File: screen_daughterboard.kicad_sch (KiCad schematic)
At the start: 18 parts, among them J7 Conn_01x24_Socket, Q4 Si1308EDL

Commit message: fixed page numbers
and adjusted some label types
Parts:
- renumbered C54 to C40, C55 to C41, C56 to C42, C57 to C43, C58 to C44, C59 to C45, C60 to C46, C61 to C47, C62 to C48, C63 to C49, D5 to D1, D6 to D2, D7 to D3, J7 to J6, L2 to L1, Q4 to Q3, R33 to R21, R34 to R23
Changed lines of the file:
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@@
+	(wire
+		(pts
+			(xy 68.58 34.29) (xy 74.93 34.29)
+		)
+		(stroke
+			(width 0)
+			(type default)
+		)
+	)
 	(wire
 		(pts
@@
 	(wire
 		(pts
+			(xy 68.58 31.75) (xy 74.93 31.75)
+		)
+		(stroke
+			(width 0)
+			(type default)
+		)
+	)
+	(wire
+		(pts
 			(xy 115.57 34.29) (xy 118.11 34.29)
 		)
@@
 	(wire
 		(pts
+			(xy 66.04 85.09) (xy 74.93 85.09)
+		)
+		(stroke
+			(width 0)
+			(type default)
+		)
+	)
+	(wire
+		(pts
 			(xy 53.34 39.37) (xy 74.93 39.37)
 		)
@@
 	(wire
 		(pts
-			(xy 132.08 41.91) (xy 130.81 41.91)
+			(xy 132.08 41.91) (xy 125.73 41.91)
 		)
 		(stroke
@@
 	(wire
 		(pts
-			(xy 175.26 81.28) (xy 176.53 81.28)
+			(xy 167.64 81.28) (xy 176.53 81.28)
 		)
 		(stroke
@@
 	(wire
 		(pts
-			(xy 146.05 71.12) (xy 147.32 71.12)
+			(xy 66.04 80.01) (xy 74.93 80.01)
+		)
+		(stroke
+			(width 0)
+			(type default)
+		)
+	)
+	(wire
+		(pts
+			(xy 137.16 71.12) (xy 147.32 71.12)
 		)
 		(stroke
@@
 	(wire
 		(pts
-			(xy 142.24 48.26) (xy 140.97 48.26)
+			(xy 147.32 48.26) (xy 140.97 48.26)
 		)
 		(stroke
@@
 		)
 	)
-	(hierarchical_label "PREVGH"
-		(shape input)
-		(at 74.93 80.01 180)
+	(label "GDR"
+		(at 125.73 41.91 0)
 		(effects
 			(font
 				(size 1.27 1.27)
 			)
-			(justify right)
-		)
-	)
-	(hierarchical_label "PREVGH"
-		(shape input)
-		(at 146.05 71.12 180)
+			(justify left bottom)
+		)
+	)
+	(label "RESE"
+		(at 147.32 48.26 180)
 		(effects
 			(font
 				(size 1.27 1.27)
 			)
-			(justify right)
+			(justify right bottom)
+		)
+	)
+	(label "PREVGH"
+		(at 66.04 80.01 0)
+		(effects
+			(font
+				(size 1.27 1.27)
+			)
+			(justify left bottom)
+		)
+	)
+	(label "PREVGL"
+		(at 167.64 81.28 0)
+		(effects
+			(font
+				(size 1.27 1.27)
+			)
+			(justify left bottom)
+		)
+	)
+	(label "RESE"
+		(at 68.58 34.29 0)
+		(effects
+			(font
+				(size 1.27 1.27)
+			)
+			(justify left bottom)
+		)
+	)
+	(label "PREVGH"
+		(at 137.16 71.12 0)
+		(effects
+			(font
+				(size 1.27 1.27)
+			)
+			(justify left bottom)
+		)
+	)
+	(label "PREVGL"
+		(at 66.04 85.09 0)
+		(effects
+			(font
+				(size 1.27 1.27)
+			)
+			(justify left bottom)
+		)
+	)
+	(label "GDR"
+		(at 68.58 31.75 0)
+		(effects
+			(font
+				(size 1.27 1.27)
+			)
+			(justify left bottom)
 		)
 	)
@@
 		)
 	)
-	(hierarchical_label "RESE"
-		(shape input)
-		(at 74.93 34.29 180)
-		(effects
-			(font
-				(size 1.27 1.27)
-			)
-			(justify right)
-		)
-	)
 	(hierarchical_label "GND"
-		(shape input)
+		(shape bidirectional)
 		(at 114.3 41.91 180)
 		(effects
@@
 		)
 	)
-	(hierarchical_label "RESE"
-		(shape input)
-		(at 142.24 48.26 0)
-		(effects
-			(font
-				(size 1.27 1.27)
-			)
-			(justify left)
-		)
-	)
-	(hierarchical_label "GDR"
-		(shape input)
-		(at 74.93 31.75 180)
-		(effects
-			(font
-				(size 1.27 1.27)
-			)
-			(justify right)
-		)
-	)
 	(hierarchical_label "DISPLAY_BUSY"
-		(shape input)
+		(shape output)
 		(at 74.93 49.53 180)
 		(effects
@@
 		)
 	)
-	(hierarchical_label "PREVGL"
-		(shape input)
-		(at 74.93 85.09 180)
-		(effects
-			(font
-				(size 1.27 1.27)
-			)
-			(justify right)
-		)
-	)
 	(hierarchical_label "DISPLAY_CS"
 		(shape input)
@@
 	)
 	(hierarchical_label "GND"
-		(shape input)
+		(shape bidirectional)
 		(at 38.1 87.63 180)
 		(effects
@@
 		)
 	)
-	(hierarchical_label "PREVGL"
-		(shape input)
-		(at 175.26 81.28 180)
-		(effects
-			(font
-				(size 1.27 1.27)
-			)
-			(justify right)
-		)
-	)
-	(hierarchical_label "GDR"
-		(shape input)
-		(at 130.81 41.91 180)
-		(effects
-			(font
-				(size 1.27 1.27)
-			)
-			(justify right)
-		)
-	)
 	(symbol
 		(lib_id "Diode:MBR0530")
@@
 		(on_board yes)
 		(dnp no)
-		(property "Reference" "D5"
+		(property "Reference" "D1"
 			(at 148.59 69.596 0)
 			(effects
@@
 		(dnp no)
 		(fields_autoplaced yes)
-		(property "Reference" "R33"
+		(property "Reference" "R21"
 			(at 134.62 50.7999 0)
 			(effects
@@
 		(dnp no)
 		(fields_autoplaced yes)
-		(property "Reference" "C60"
+		(property "Reference" "C46"
 			(at 118.11 36.8235 0)
 			(effects
@@
 		(dnp no)
 		(fields_autoplaced yes)
-		(property "Reference" "J7"
+		(property "Reference" "J6"
 			(at 81.28 57.1499 0)
 			(effects
@@
 		(dnp no)
 		(fields_autoplaced yes)
-		(property "Reference" "#PWR099"
+		(property "Reference" "#PWR075"
 			(at 147.32 86.36 0)
 			(effects
@@
 		(dnp no)
 		(fields_autoplaced yes)
-		(property "Reference" "#PWR094"
+		(property "Reference" "#PWR073"
 			(at 115.57 49.53 0)
 			(effects
@@
 		(dnp no)
 		(fields_autoplaced yes)
-		(property "Reference" "#PWR0100"
+		(property "Reference" "#PWR076"
 			(at 157.48 88.9 0)
 			(effects
@@
 		(dnp no)
 		(fields_autoplaced yes)
-		(property "Reference" "C56"
+		(property "Reference" "C42"
 			(at 49.5363 76.2 90)
 			(effects
@@
 		(dnp no)
 		(fields_autoplaced yes)
-		(property "Reference" "C59"
+		(property "Reference" "C45"
 			(at 57.1563 81.28 90)
 			(effects
@@
 		(dnp no)
 		(fields_autoplaced yes)
-		(property "Reference" "L2"
+		(property "Reference" "L1"
 			(at 120.65 29.21 90)
 			(effects
@@
 		(dnp no)
 		(fields_autoplaced yes)
-		(property "Reference" "C58"
+		(property "Reference" "C44"
 			(at 57.1563 71.12 90)
 			(effects
@@
 		(dnp no)
 		(fields_autoplaced yes)
-		(property "Reference" "R34"
+		(property "Reference" "R23"
 			(at 143.51 50.7999 0)
 			(effects
@@
 		(on_board yes)
 		(dnp no)
-		(property "Reference" "D7"
+		(property "Reference" "D3"
 			(at 178.562 79.502 0)
 			(effects
@@
 		(dnp no)
 		(fields_autoplaced yes)
-		(property "Reference" "Q4"
+		(property "Reference" "Q3"
 			(at 144.78 40.6399 0)
 			(effects
@@
 		(dnp no)
 		(fields_autoplaced yes)
-		(property "Reference" "C61"
+		(property "Reference" "C47"
 			(at 149.86 73.6535 0)
 			(effects
@@
 		(dnp no)
 		(fields_autoplaced yes)
-		(property "Reference" "C62"
+		(property "Reference" "C48"
 			(at 160.02 63.4935 0)
 			(effects
@@
 		(dnp no)
 		(fields_autoplaced yes)
-		(property "Reference" "#PWR098"
+		(property "Reference" "#PWR074"
 			(at 140.97 63.5 0)
 			(effects
@@
 		(on_board yes)
 		(dnp no)
-		(property "Reference" "D6"
+		(property "Reference" "D2"
 			(at 158.75 81.026 0)
 			(effects
@@
 		(dnp no)
 		(fields_autoplaced yes)
-		(property "Reference" "C63"
+		(property "Reference" "C49"
 			(at 179.07 83.8135 0)
 			(effects
@@
 		(dnp no)
 		(fields_autoplaced yes)
-		(property "Reference" "#PWR089"
+		(property "Reference" "#PWR065"
 			(at 55.88 63.5 0)
 			(effects
@@
 		(dnp no)
 		(fields_autoplaced yes)
-		(property "Reference" "C55"
+		(property "Reference" "C41"
 			(at 49.5363 66.04 90)
 			(effects
@@
 		(dnp no)
 		(fields_autoplaced yes)
-		(property "Reference" "#PWR091"
+		(property "Reference" "#PWR072"
 			(at 119.38 33.02 0)
 			(effects
@@
 		(dnp no)
 		(fields_autoplaced yes)
-		(property "Reference" "#PWR0101"
+		(property "Reference" "#PWR077"
 			(at 176.53 96.52 0)
 			(effects
@@
 		(dnp no)
 		(fields_autoplaced yes)
-		(property "Reference" "C57"
+		(property "Reference" "C43"
 			(at 50.8063 33.02 90)
 			(effects
@@
 		(dnp no)
 		(fields_autoplaced yes)
-		(property "Reference" "#PWR088"
+		(property "Reference" "#PWR050"
 			(at 39.37 96.52 0)
 			(effects
@@
 		(dnp no)
 		(fields_autoplaced yes)
-		(property "Reference" "C54"
+		(property "Reference" "C40"
 			(at 45.7263 58.42 90)
 			(effects

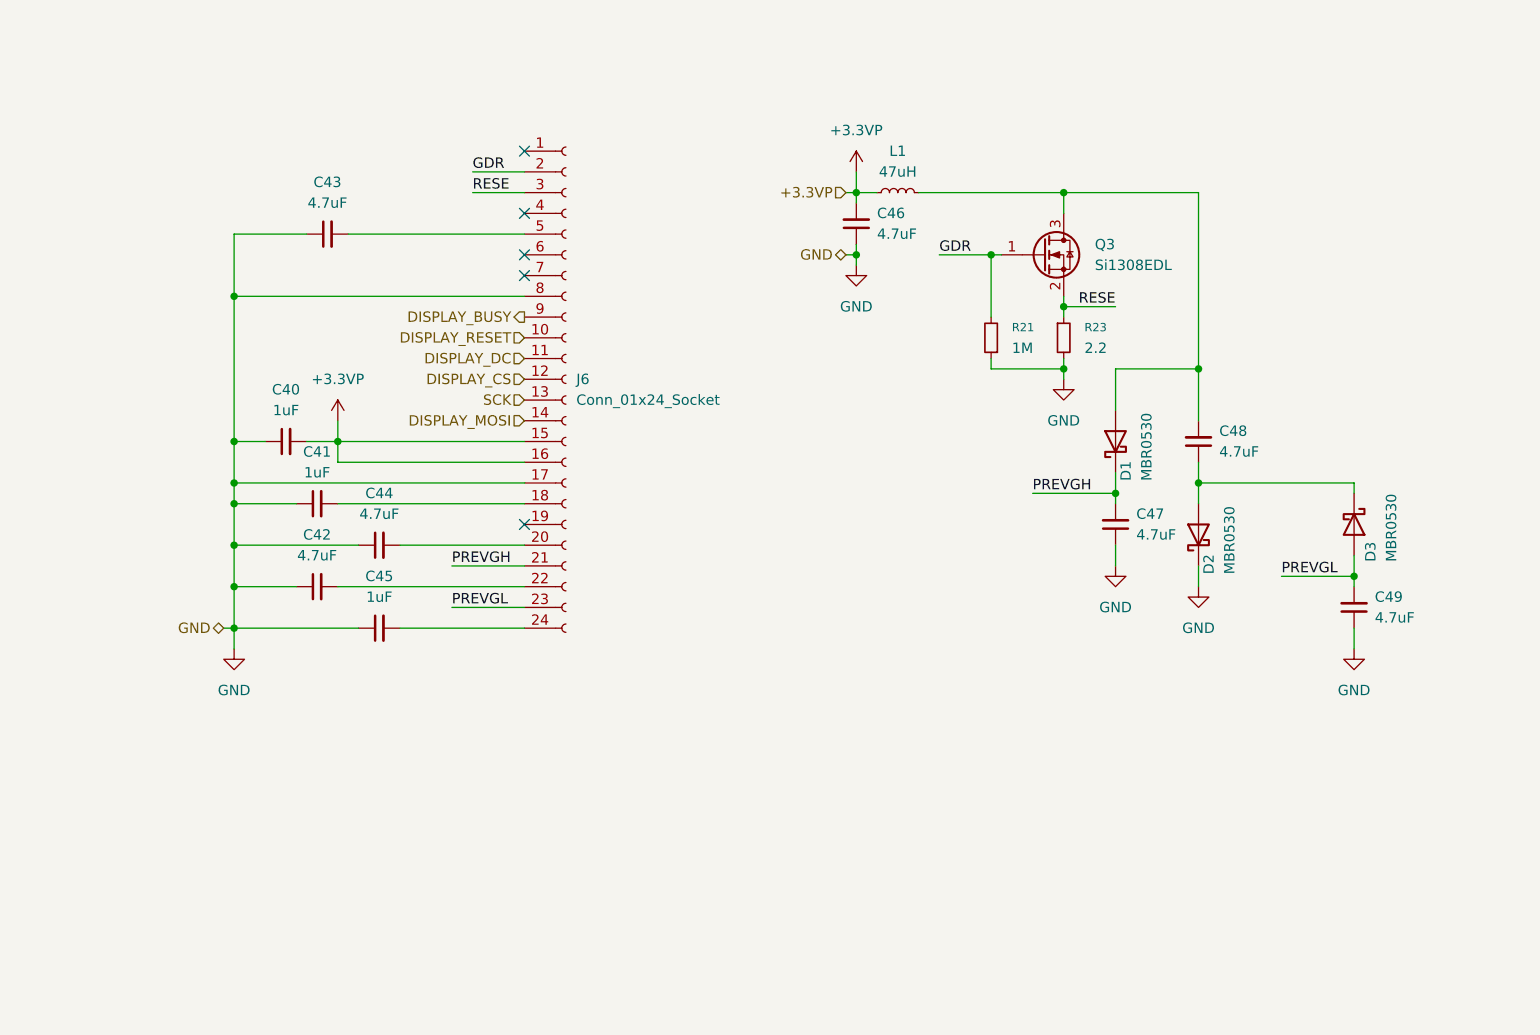
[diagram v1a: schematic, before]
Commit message: separating schematics based on board
finished splitting every component up into separate sheets in the schematic based on what physical board it's going on
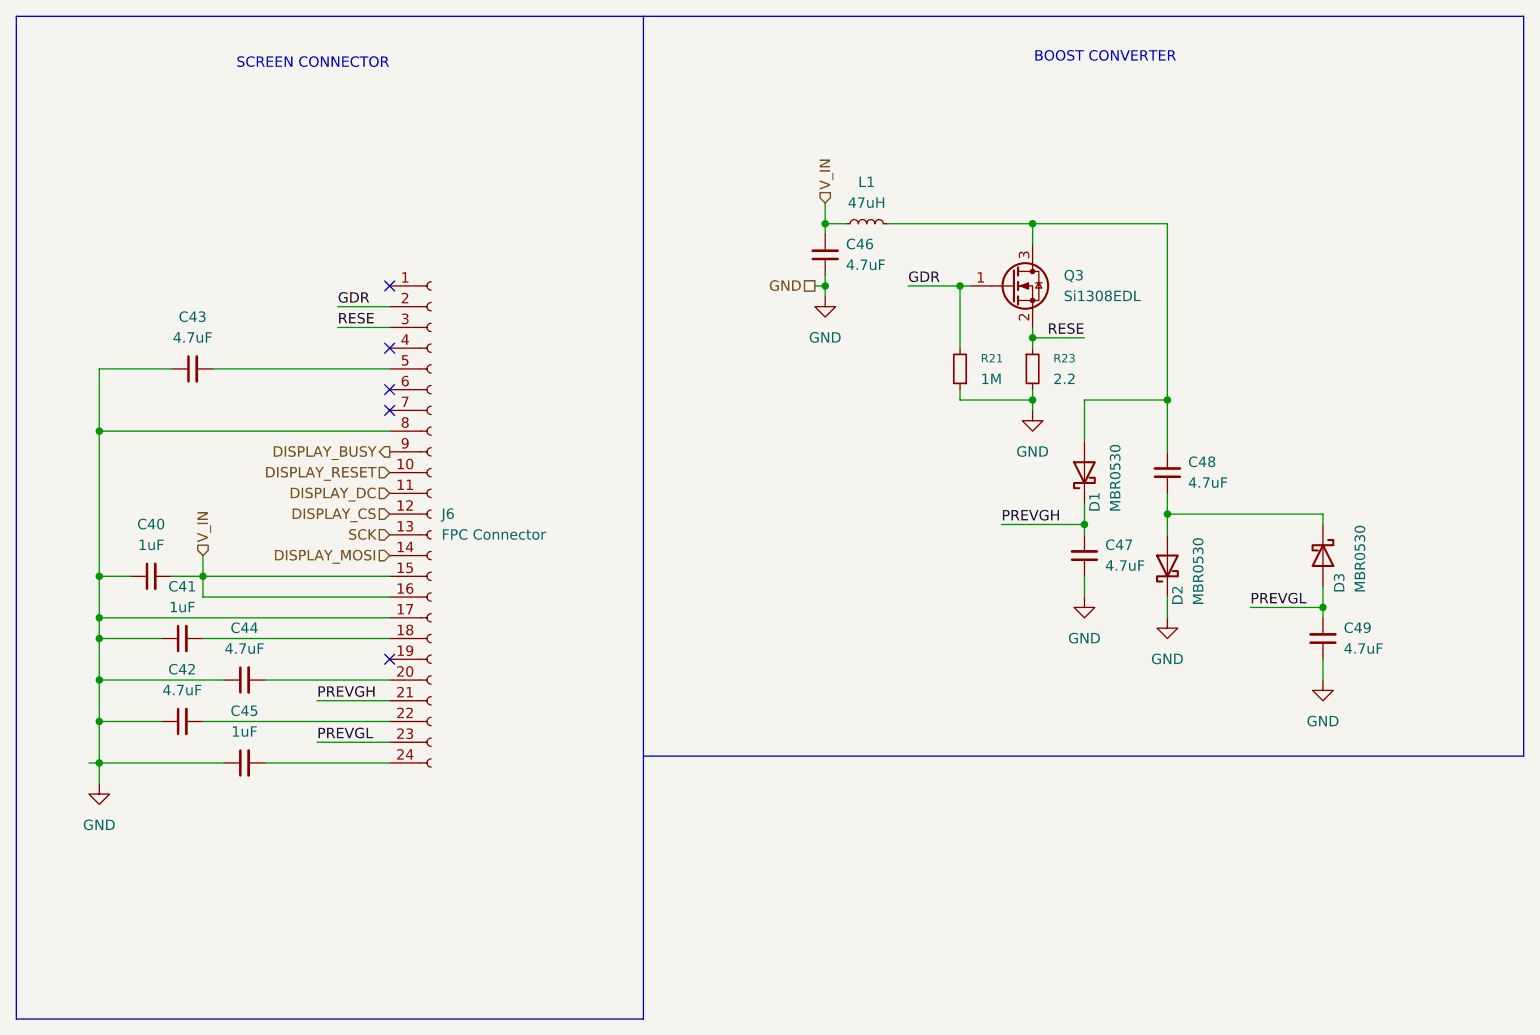
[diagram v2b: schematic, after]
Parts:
- J6: value Conn_01x24_Socket -> FPC Connector
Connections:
- net +3.3VP renamed V_IN
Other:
- note added: "BOOST CONVERTER"
- note added: "SCREEN CONNECTOR"
- moved on the sheet: C40, C41, C42, C43, C44, C45, C46, C47, C48, C49, D1, D2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

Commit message: assigning pcb footprints
assigned pcb footprints to most components:

- rotary encoder footprint will need slight modification to fit bourns PEC11L

- need to finalize components for reset button and the four switches before assigning those footprints
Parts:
- C40, C41, C42, C43, C44, C45, C46, C47, C48, C49: footprint (none) -> Capacitor_SMD:C_0805_2012Metric
- J6: footprint (none) -> Connector_FFC-FPC:Hirose_FH12-24S-0.5SH_1x24-1MP_P0.50mm_Horizontal
- L1: footprint (none) -> Inductor_SMD:L_APV_ANR3015
- R21: footprint (none) -> Resistor_SMD:R_0805_2012Metric
- R23: footprint (none) -> Resistor_SMD:R_0603_1608Metric
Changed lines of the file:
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@@
 			)
 		)
-		(property "Footprint" ""
+		(property "Footprint" "Resistor_SMD:R_0805_2012Metric"
 			(at 128.27 55.88 0)
 			(effects
@@
 			)
 		)
-		(property "Footprint" ""
+		(property "Footprint" "Capacitor_SMD:C_0805_2012Metric"
 			(at 111.76 41.91 0)
 			(effects
@@
 			)
 		)
-		(property "Footprint" ""
+		(property "Footprint" "Connector_FFC-FPC:Hirose_FH12-24S-0.5SH_1x24-1MP_P0.50mm_Horizontal"
 			(at 63.5 73.66 0)
 			(effects
@@
 			)
 		)
-		(property "Footprint" ""
+		(property "Footprint" "Capacitor_SMD:C_0805_2012Metric"
 			(at 33.02 99.06 0)
 			(effects
@@
 			)
 		)
-		(property "Footprint" ""
+		(property "Footprint" "Capacitor_SMD:C_0805_2012Metric"
 			(at 40.64 104.14 0)
 			(effects
@@
 			)
 		)
-		(property "Footprint" ""
+		(property "Footprint" "Inductor_SMD:L_APV_ANR3015"
 			(at 116.84 38.1 0)
 			(effects
@@
 			)
 		)
-		(property "Footprint" ""
+		(property "Footprint" "Capacitor_SMD:C_0805_2012Metric"
 			(at 40.64 93.98 0)
 			(effects
@@
 			)
 		)
-		(property "Footprint" ""
+		(property "Footprint" "Resistor_SMD:R_0603_1608Metric"
 			(at 137.16 55.88 0)
 			(effects
@@
 			)
 		)
-		(property "Footprint" ""
+		(property "Footprint" "Capacitor_SMD:C_0805_2012Metric"
 			(at 143.51 78.74 0)
 			(effects
@@
 			)
 		)
-		(property "Footprint" ""
+		(property "Footprint" "Capacitor_SMD:C_0805_2012Metric"
 			(at 153.67 68.58 0)
 			(effects
@@
 			)
 		)
-		(property "Footprint" ""
+		(property "Footprint" "Capacitor_SMD:C_0805_2012Metric"
 			(at 172.72 88.9 0)
 			(effects
@@
 			)
 		)
-		(property "Footprint" ""
+		(property "Footprint" "Capacitor_SMD:C_0805_2012Metric"
 			(at 33.02 88.9 0)
 			(effects
@@
 			)
 		)
-		(property "Footprint" ""
+		(property "Footprint" "Capacitor_SMD:C_0805_2012Metric"
 			(at 34.29 55.88 0)
 			(effects
@@
 			)
 		)
-		(property "Footprint" ""
+		(property "Footprint" "Capacitor_SMD:C_0805_2012Metric"
 			(at 29.21 81.28 0)
 			(effects

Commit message: finalizing schematics
connected the new DAC footprint, filled in title blocks
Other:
- company: (none) -> rien+la_reine;
- title: (none) -> Tome: Display Daughterboard

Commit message: updating schematic
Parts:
- renumbered C40 to C401, C41 to C402, C42 to C403, C43 to C404, C44 to C405, C45 to C406, C46 to C407, C47 to C408, C48 to C409, C49 to C410, D1 to D401, D2 to D402, D3 to D403, J6 to J401, L1 to L401, Q3 to Q401, R21 to R401, R23 to R402
